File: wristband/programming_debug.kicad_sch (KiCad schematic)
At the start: 1 part, among them J3 Conn_ARM_JTAG_SWD_10

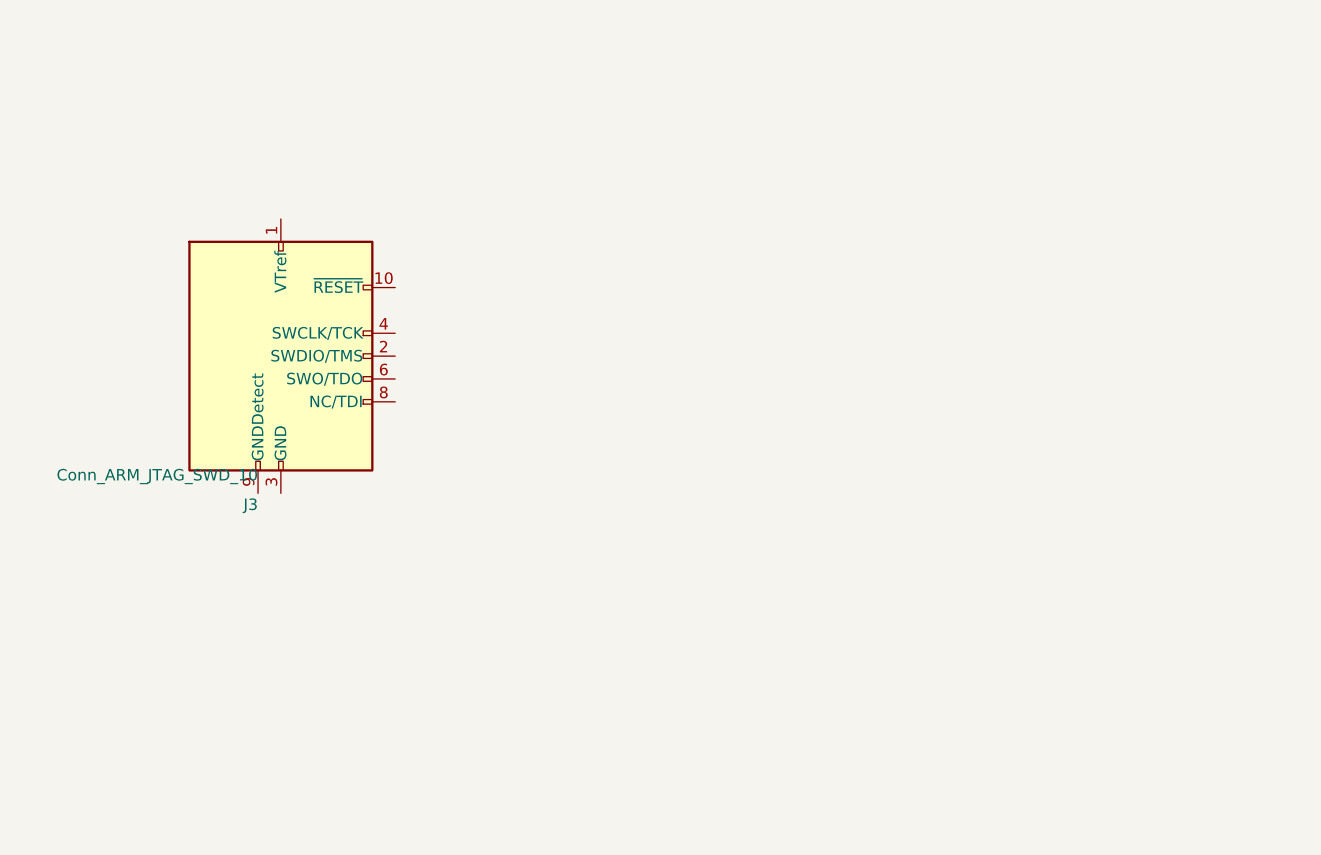
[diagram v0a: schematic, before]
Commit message: Land the wristband branch on main: DWM3001C wiring, TPS7A02 LDO, PCB (#5)
Brings six months of `dwm3001c-migration` onto current `main` as one commit.
A true rebase was attempted first and abandoned: the branch's own first
commit is a NINA-B400 migration that commit five then throws away, so
replaying it meant resolving 16 files of conflict for a design state nobody
wants. Squashed to a single three-way merge instead -- 18 conflicts, one
pass.

Both sides had independently migrated the wristband to the DWM3001C, so this
was not a fast-forward. Resolution, by ERC evidence rather than recency:

  main's wristband     104 violations, 93 errors
  branch's wristband     1 violation,   0 errors

main's 93 are 80 pin_not_connected + 10 power_pin_not_driven + 3
pin_not_driven -- PR #1 swapped in a fresh radio sheet and never wired it.
The branch wired it. So the branch's schematics are the base here, not
main's.

Taken from the branch: radio_mcu, regulation, programming_debug,
power_bms, mechanical, libs/, the PCB (9.8k lines, main has none), and the
DWM3001C footprint placeholder.

Taken from main: all project-wide docs. The branch's were stale on the bay
station -- still ESP32-S3 and DWM3000, which main replaced with BT840 and
DW3210.

Reconciled by hand:
- wristband.kicad_sch now carries main's 7-sheet hierarchy. `antenna` is
  dropped (DWM3001C has both antennas on-module); `indicators` and
  `testpoints` are spliced in from main verbatim, UUIDs preserved, so their
  child sheets' instance paths still resolve -- both roots share the root
  UUID b3417696, and the paths check out.
- decisions.md, passives-reference.md and wristband/README.md carried main's
  MCP1700 as the wristband LDO. Rewritten for the TPS7A02, with the swap's
  rationale ported from the branch rather than restated.
- README sheet table corrected: main marked every sheet "Placement only",
  which is no longer true for the five the branch wired.
- Dropped NINA-B400-55_PLACEHOLDER.kicad_mod; that part is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
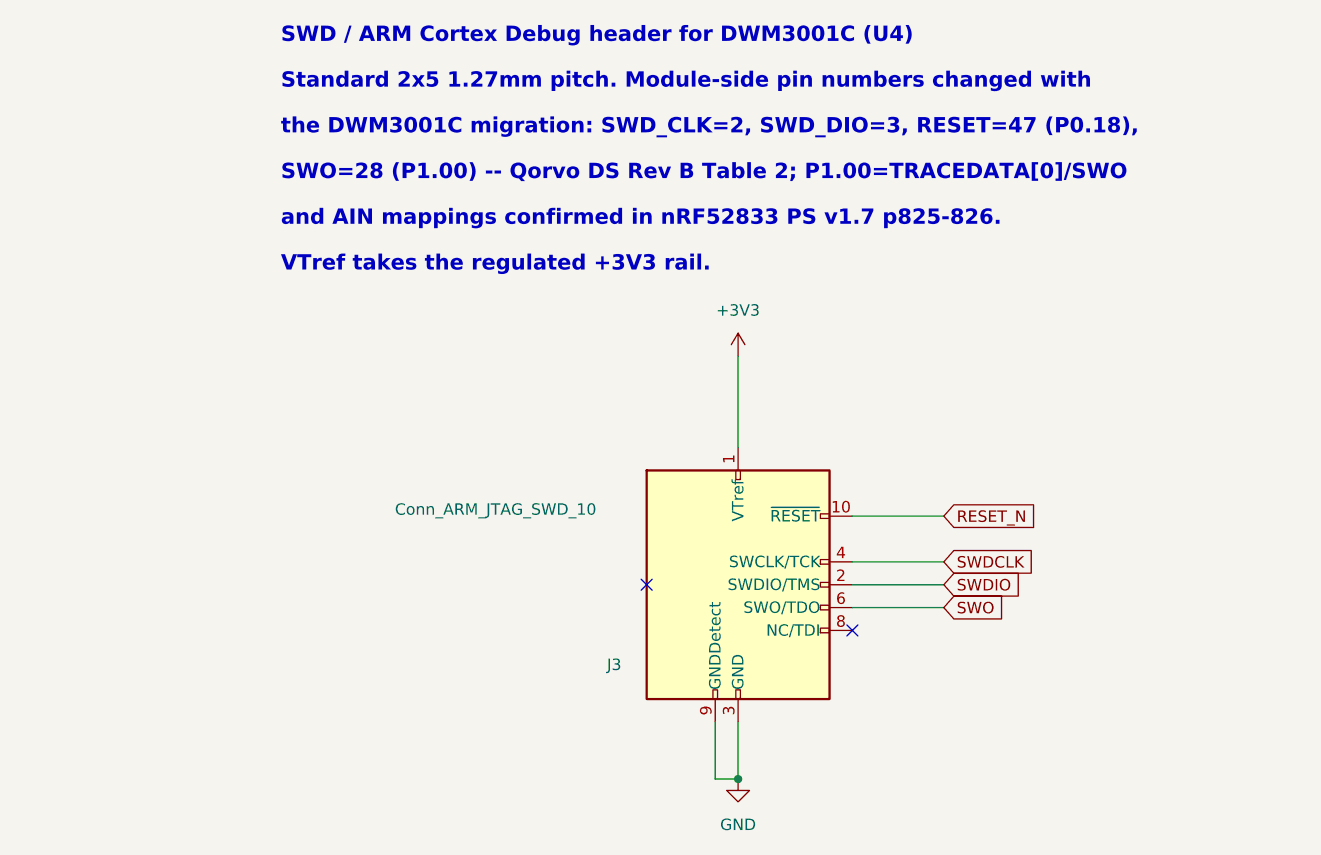
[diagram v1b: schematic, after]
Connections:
- net +3V3: now reaches J3.1 (VTref)
- net RESET_N: now reaches J3.10 (~{RESET})
- net SWDIO: now reaches J3.2 (SWDIO/TMS)
- net GND: now reaches J3.3 (GND), J3.5 (GND)
- net GND: now also J3.9 (GNDDetect)
- net SWDCLK: now reaches J3.4 (SWCLK/TCK)
- net SWO: now reaches J3.6 (SWO/TDO)
- no-connect marks 0 -> 2
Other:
- note added: "SWD / ARM Cortex Debug header for DWM3001C (U4)"
- note added: "SWO=28 (P1.00) -- Qorvo DS Rev B Table 2; P1.00=TRACEDATA[0]/SWO"
- note added: "Standard 2x5 1.27mm pitch. Module-side pin numbers changed with"
- note added: "VTref takes the regulated +3V3 rail."
- note added: "and AIN mappings confirmed in nRF52833 PS v1.7 p825-826."
- note added: "the DWM3001C migration: SWD_CLK=2, SWD_DIO=3, RESET=47 (P0.18),"
- moved on the sheet: J3
